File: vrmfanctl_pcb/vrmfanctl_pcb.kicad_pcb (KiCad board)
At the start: 2 copper layers, 27.9 x 22.9 mm, 6 parts, among them J1 SATA Power Male, J2 Through Hole, J3 Pin socket L-shape, J4 Pin socket L-shape, U1 ATtiny85-20PU

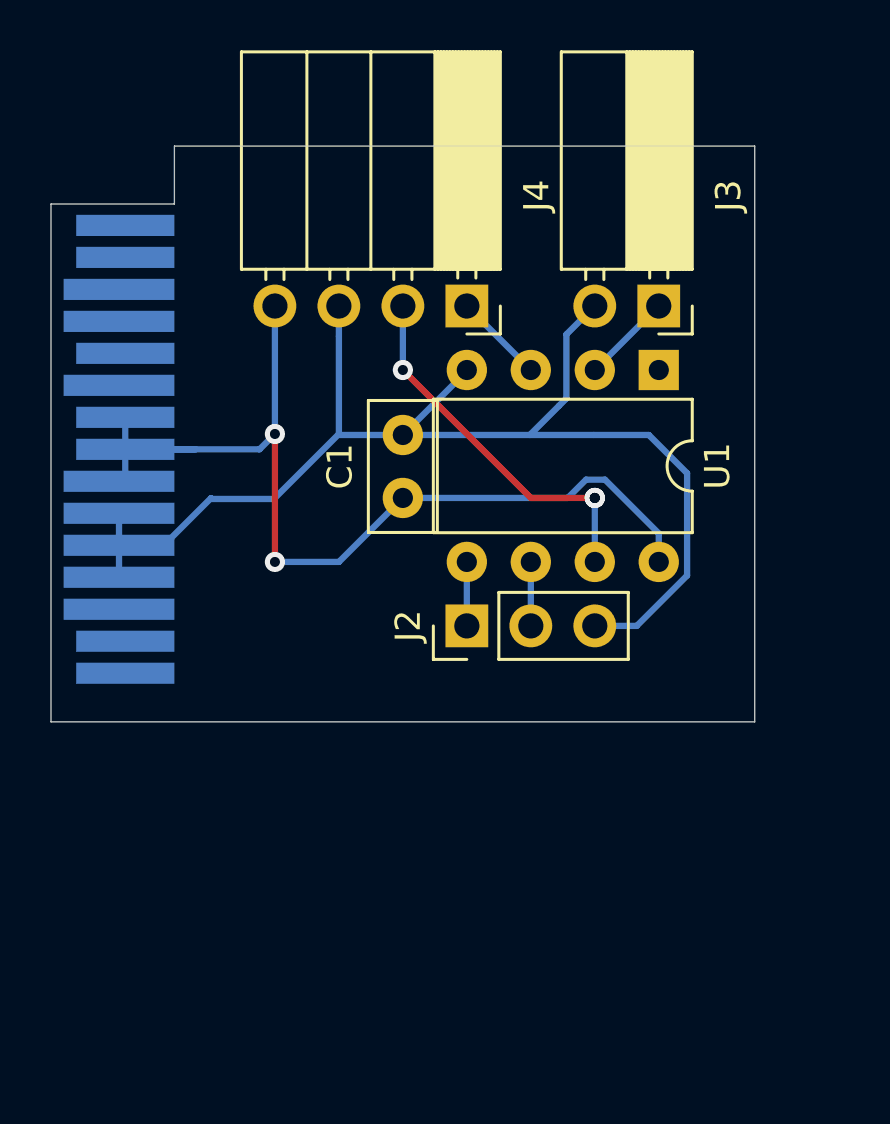
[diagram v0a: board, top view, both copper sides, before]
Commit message: change pcb layout
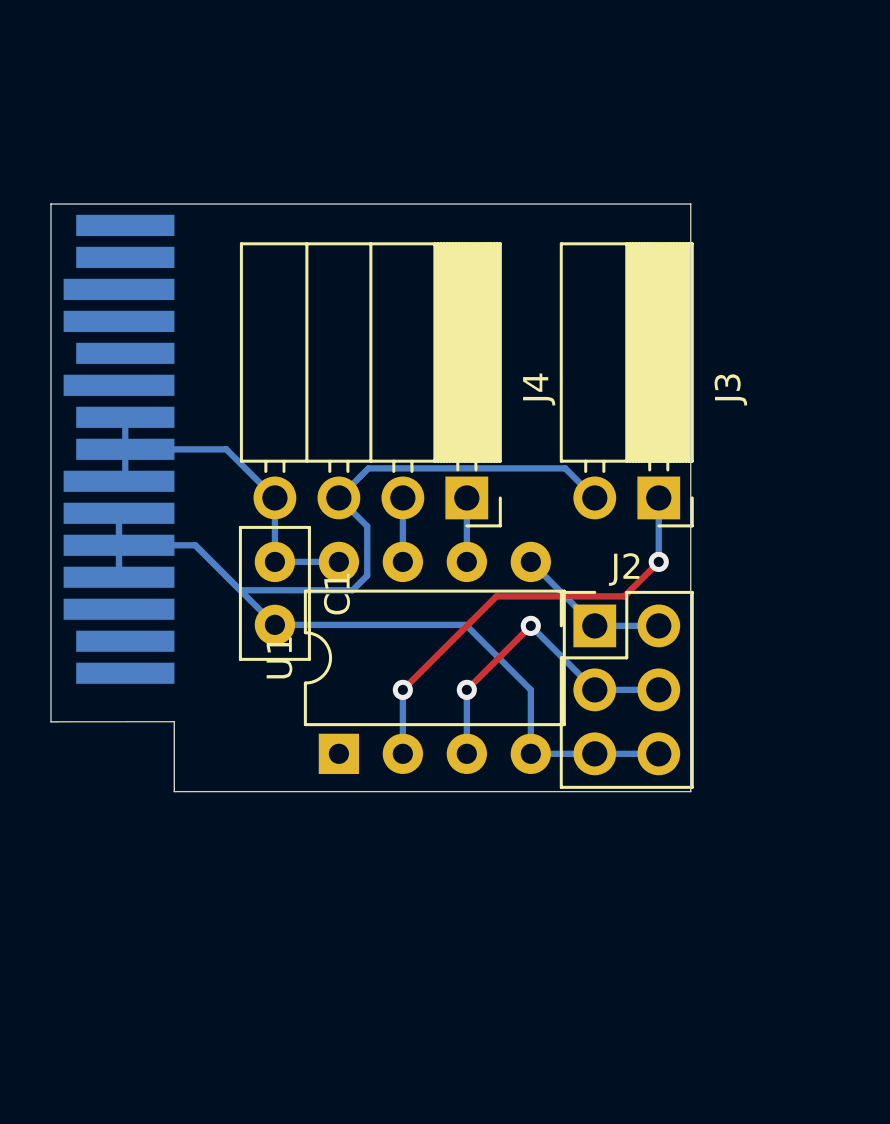
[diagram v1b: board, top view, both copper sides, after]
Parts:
- J2: value Through Hole -> Conn_02x03_Odd_Even; footprint Connector_PinHeader_2.54mm:PinHeader_1x03_P2.54mm_Vertical -> Connector_PinHeader_2.54mm:PinHeader_2x03_P2.54mm_Vertical
- moved U1 19.8 mm to (48.3, 63.5), turned to 90 degrees
- moved J3 7.62 mm to (61.0, 53.3)
- moved J4 7.62 mm to (53.3, 53.3)
- moved C1 5.68 mm to (45.7, 55.9), turned to 270 degrees
- moved J2 5.08 mm to (58.4, 58.4), turned to 0 degrees
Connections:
- J2 pad 2: /RX -> /TX
- J2 pad 3: GND -> /RX
- U1 pad 3: /PWM -> /RX
- U1 pad 6: /RX -> /PWM
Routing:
- net VCC: track 41.9 -> 16.0 mm, vias 2 -> 0
- net /D+: track 3.59 -> 17.3 mm, vias 0 -> 2
- net /FG: track 14.8 -> 2.54 mm, vias 3 -> 0
- net /RX: track 2.54 -> 12.3 mm, vias 0 -> 2
- net /TX: track 2.54 -> 6.13 mm
- net /PWM: track 3.59 -> 2.54 mm
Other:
- board size 27.9 x 22.9 mm -> 25.4 x 23.3 mm

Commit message: change temperature measurement method. remove configuration interface. use printf instead of put*.
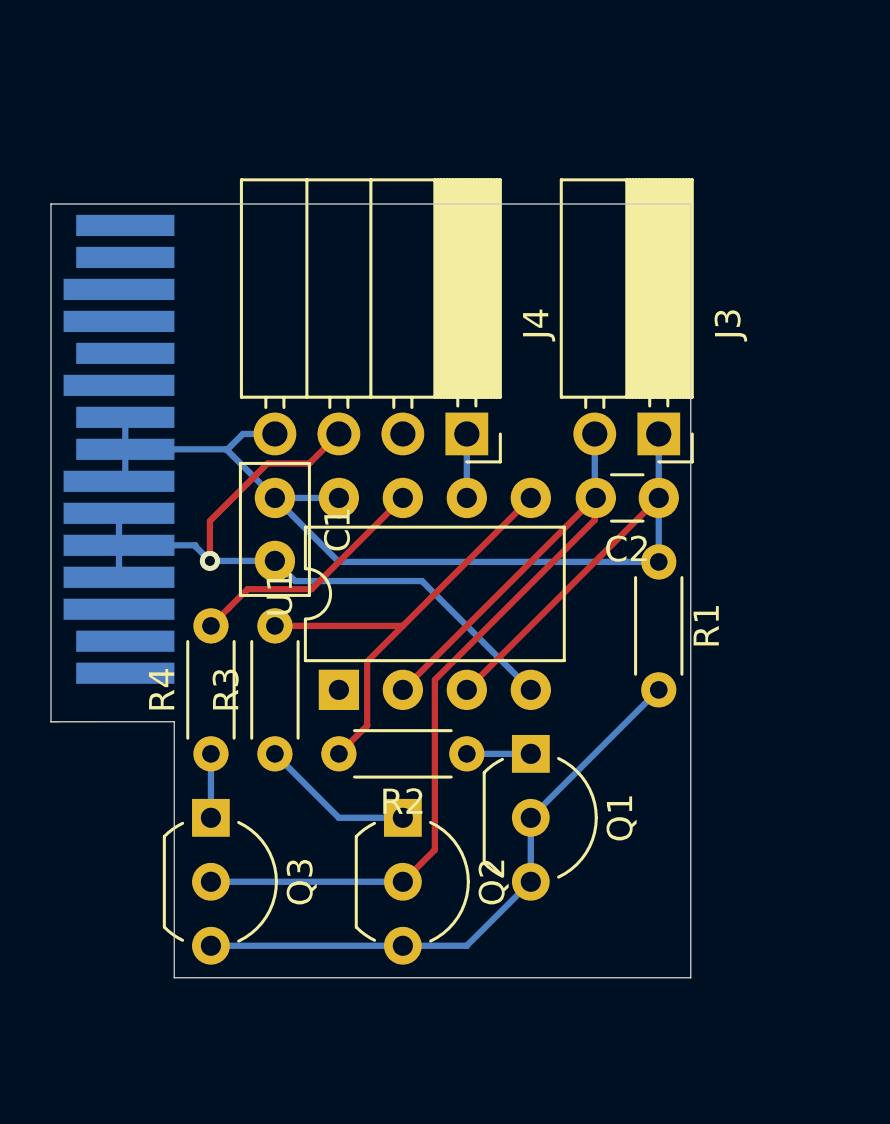
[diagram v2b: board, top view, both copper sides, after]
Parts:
- removed J2: Conn_02x03_Odd_Even, Connector_PinHeader_2.54mm:PinHeader_2x03_P2.54mm_Vertical
- added C2: 470p, Capacitor_THT:C_Disc_D3.0mm_W1.6mm_P2.50mm, F.Cu at (61.0, 53.3)
- added Q1: 2SC1740, Package_TO_SOT_THT:TO-92_Inline_Wide, F.Cu at (55.9, 63.5)
- added Q2: 2SC1740, Package_TO_SOT_THT:TO-92_Inline_Wide, F.Cu at (50.8, 66.0)
- added Q3: 2SC1740, Package_TO_SOT_THT:TO-92_Inline_Wide, F.Cu at (43.2, 66.0)
- added R1: 56k, Resistor_THT:R_Axial_DIN0204_L3.6mm_D1.6mm_P5.08mm_Horizontal, F.Cu at (61.0, 55.9)
- added R2: 390k, Resistor_THT:R_Axial_DIN0204_L3.6mm_D1.6mm_P5.08mm_Horizontal, F.Cu at (53.3, 63.5)
- added R3: 390k, Resistor_THT:R_Axial_DIN0204_L3.6mm_D1.6mm_P5.08mm_Horizontal, F.Cu at (45.7, 63.5)
- added R4: 20k, Resistor_THT:R_Axial_DIN0204_L3.6mm_D1.6mm_P5.08mm_Horizontal, F.Cu at (43.2, 63.5)
- moved J3 2.54 mm to (61.0, 50.8)
- moved J4 2.54 mm to (53.3, 50.8)
- moved C1 2.54 mm to (45.7, 53.3)
- moved U1 2.54 mm to (48.3, 61.0)
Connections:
- J3 pad 1: /D+ -> VCC
- J3 pad 2: GND -> /D-
- J4 pad 2: /FG -> (no net)
- U1 pad 2: /D+ -> /D-
- U1 pad 3: /RX -> VCC
- U1 pad 5: /TX -> /BDPWR10
- U1 pad 7: /FG -> /BDPWR200
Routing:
- net /D-: track 0.00 -> 39.4 mm
- net VCC: track 16.0 -> 47.8 mm
- net Net-(Q1-Pad2): track 0.00 -> 23.5 mm
- net GND: track 53.1 -> 31.2 mm, vias 0 -> 1
- net /BDPWR10: track 0.00 -> 18.4 mm
- net /D+: track 17.3 -> 0.00 mm, vias 2 -> 0
- net /RX: track 12.3 -> 0.00 mm, vias 2 -> 0
- net /BDPWR200: track 0.00 -> 9.72 mm
- net Net-(Q2-Pad1): track 0.00 -> 6.13 mm
- net /TX: track 6.13 -> 0.00 mm
- net Net-(Q3-Pad1): track 0.00 -> 2.54 mm
- net Net-(Q1-Pad1): track 0.00 -> 2.54 mm
- net /FG: track 2.54 -> 0.00 mm
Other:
- board size 25.4 x 23.3 mm -> 25.4 x 30.7 mm

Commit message: swap BDPWR10 and TX. Add UART pin header
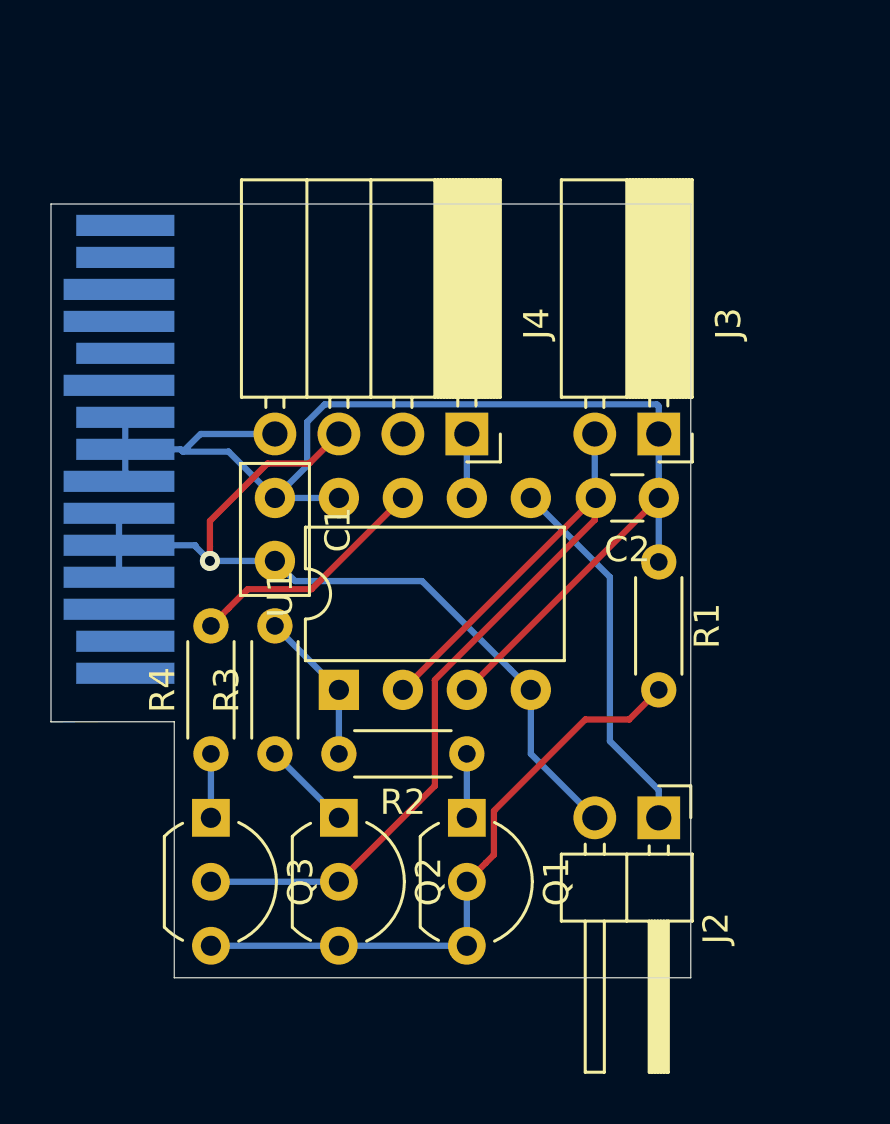
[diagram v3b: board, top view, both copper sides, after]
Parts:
- added J2: Pin header L-shape, Connector_PinHeader_2.54mm:PinHeader_1x02_P2.54mm_Horizontal, F.Cu at (61.0, 66.0)
- moved Q1 3.59 mm to (53.3, 66.0)
- moved Q2 2.54 mm to (48.3, 66.0)
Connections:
- J1 pad 1: (no net) -> Net-(J1-Pad1)
- J1 pad 10: (no net) -> Net-(J1-Pad10)
- J1 pad 11: (no net) -> Net-(J1-Pad11)
- J1 pad 12: (no net) -> Net-(J1-Pad12)
- J1 pad 13: (no net) -> Net-(J1-Pad13)
- J1 pad 14: (no net) -> Net-(J1-Pad14)
- J1 pad 15: (no net) -> Net-(J1-Pad15)
- J1 pad 2: (no net) -> Net-(J1-Pad2)
- J1 pad 3: (no net) -> Net-(J1-Pad3)
- J4 pad 2: (no net) -> Net-(J4-Pad2)
- U1 pad 1: (no net) -> /BDPWR10
- U1 pad 5: /BDPWR10 -> /TX_RX
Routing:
- net /TX_RX: track 0.00 -> 14.8 mm
- net /BDPWR10: track 18.4 -> 6.13 mm
- net GND: track 31.2 -> 37.3 mm
- net VCC: track 47.8 -> 52.2 mm
- net Net-(Q2-Pad1): track 6.13 -> 3.59 mm
- net /D-: track 39.4 -> 37.9 mm
- net Net-(Q1-Pad2): track 23.5 -> 24.5 mm

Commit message: keep analog signals from digital signals
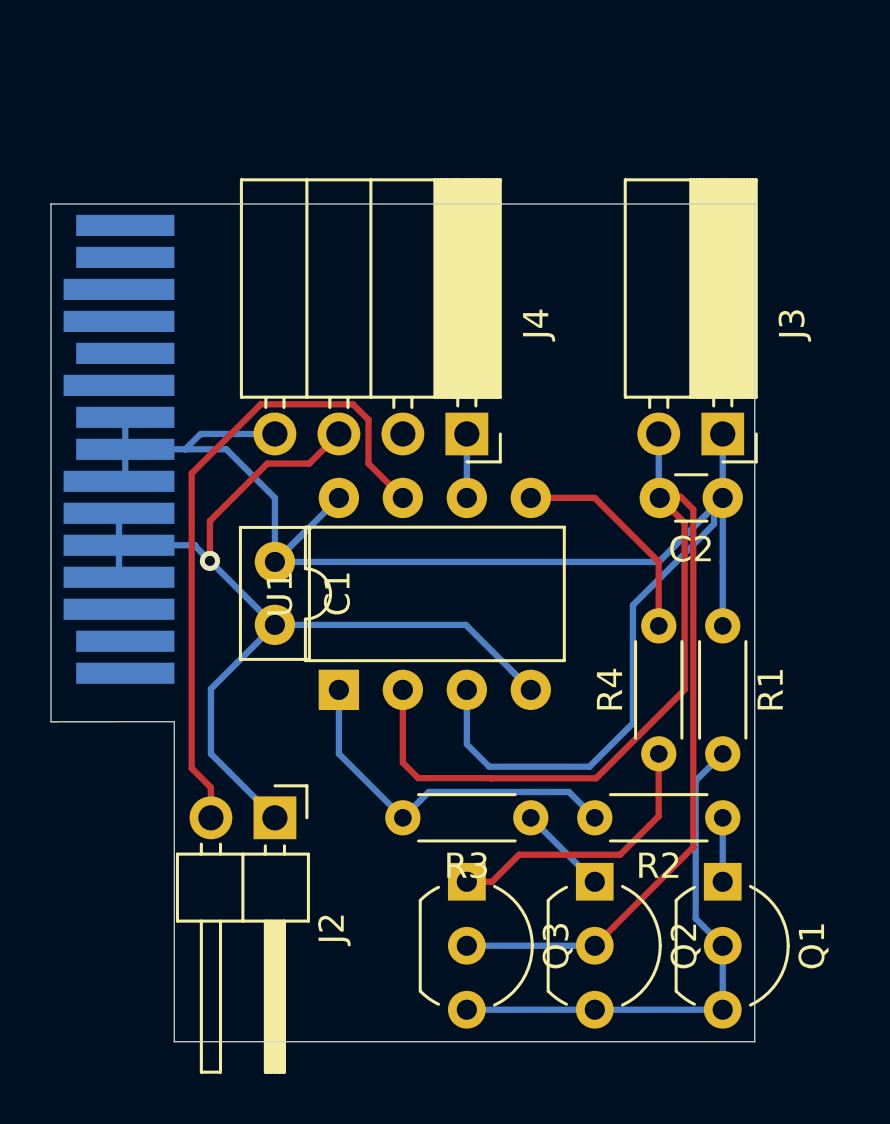
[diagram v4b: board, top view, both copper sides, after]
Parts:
- moved R4 17.8 mm to (61.0, 63.5)
- moved J2 15.2 mm to (45.7, 66.0)
- moved R3 10.5 mm to (55.9, 66.0), turned to 180 degrees
- moved Q2 10.5 mm to (58.4, 68.6)
- moved Q3 10.5 mm to (53.3, 68.6)
- moved R2 10.5 mm to (63.5, 66.0)
- moved Q1 10.5 mm to (63.5, 68.6)
- moved R1 3.59 mm to (63.5, 58.4)
- moved C1 2.54 mm to (45.7, 55.9)
- moved C2 2.54 mm to (63.5, 53.3)
- moved J3 2.54 mm to (63.5, 50.8)
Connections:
- J1 pad 1: Net-(J1-Pad1) -> (no net)
- J1 pad 10: Net-(J1-Pad10) -> (no net)
- J1 pad 11: Net-(J1-Pad11) -> (no net)
- J1 pad 12: Net-(J1-Pad12) -> (no net)
- J1 pad 13: Net-(J1-Pad13) -> (no net)
- J1 pad 14: Net-(J1-Pad14) -> (no net)
- J1 pad 15: Net-(J1-Pad15) -> (no net)
- J1 pad 2: Net-(J1-Pad2) -> (no net)
- J1 pad 3: Net-(J1-Pad3) -> (no net)
- J2 pad 1: /TX_RX -> GND
- J2 pad 2: GND -> /TX_RX
- J4 pad 2: Net-(J4-Pad2) -> (no net)
- U1 pad 5: /TX_RX -> /BDPWR200
- U1 pad 7: /BDPWR200 -> /TX_RX
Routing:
- net VCC: track 52.2 -> 69.6 mm
- net /D-: track 37.9 -> 52.1 mm
- net /TX_RX: track 14.8 -> 26.1 mm
- net Net-(Q3-Pad1): track 2.54 -> 11.2 mm
- net /BDPWR10: track 6.13 -> 14.6 mm
- net GND: track 37.3 -> 42.1 mm
- net Net-(Q1-Pad2): track 24.5 -> 21.2 mm
- net /BDPWR200: track 9.72 -> 8.67 mm
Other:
- board size 25.4 x 30.7 mm -> 27.9 x 33.3 mm
